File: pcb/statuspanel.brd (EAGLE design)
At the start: 57.1 x 66 mm, 8 parts

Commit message: Bump the version number.
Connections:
- net GND: now also DISPLAY.39
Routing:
- net GND: track 81.1 -> 89.8 mm
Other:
- board text added: "StatusPanel v0.3"
- board text removed: "StatusPanel v0.2"
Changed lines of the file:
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@@
 <hole x="21.59" y="4.445" drill="2.54"/>
 <hole x="3.81" y="4.445" drill="2.54"/>
-<text x="55.88" y="40.64" size="1.778" layer="25" rot="R90">StatusPanel v0.2</text>
+<text x="55.88" y="40.64" size="1.778" layer="25" rot="R90">StatusPanel v0.3</text>
 <hole x="53.34" y="62.23" drill="2.54"/>
 <hole x="53.34" y="3.81" drill="2.54"/>
@@
 <wire x1="29.2608" y1="44.3484" x2="29.21" y2="44.45" width="0.1524" layer="1"/>
 <wire x1="31.6992" y1="39.4716" x2="31.75" y2="39.37" width="0.1524" layer="1"/>
+<contactref element="DISPLAY" pad="39"/>
+<wire x1="31.6992" y1="56.0832" x2="31.6992" y2="57.15" width="0.1524" layer="1"/>
+<wire x1="30.3276" y1="54.7116" x2="31.6992" y2="56.0832" width="0.1524" layer="1"/>
+<wire x1="30.3276" y1="50.5968" x2="30.3276" y2="54.7116" width="0.1524" layer="1"/>
+<wire x1="29.2608" y1="49.53" x2="30.3276" y2="50.5968" width="0.1524" layer="1"/>
+<wire x1="31.6992" y1="57.15" x2="31.75" y2="57.15" width="0.1524" layer="1"/>
+<wire x1="29.2608" y1="49.53" x2="29.21" y2="49.53" width="0.1524" layer="1"/>
 </signal>
 <signal name="AUTO">

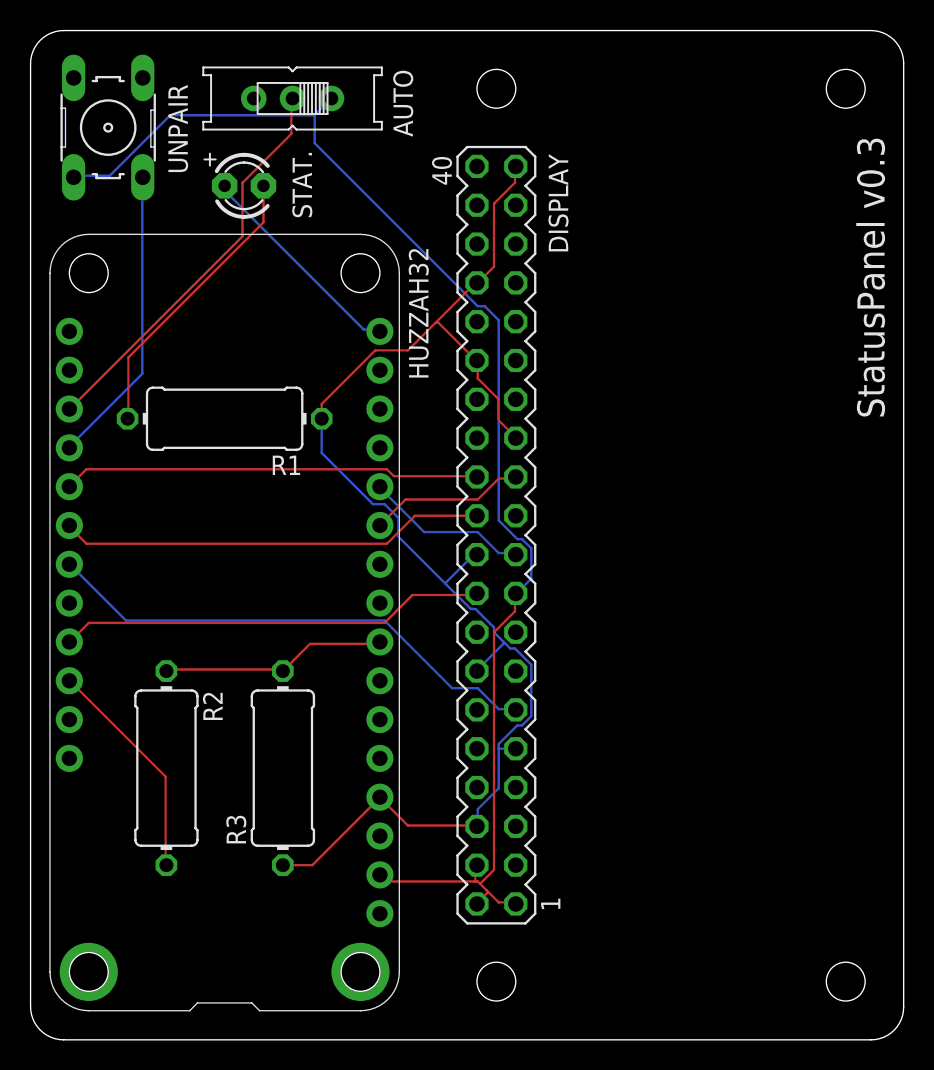
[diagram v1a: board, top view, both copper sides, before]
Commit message: Change the busy pin.
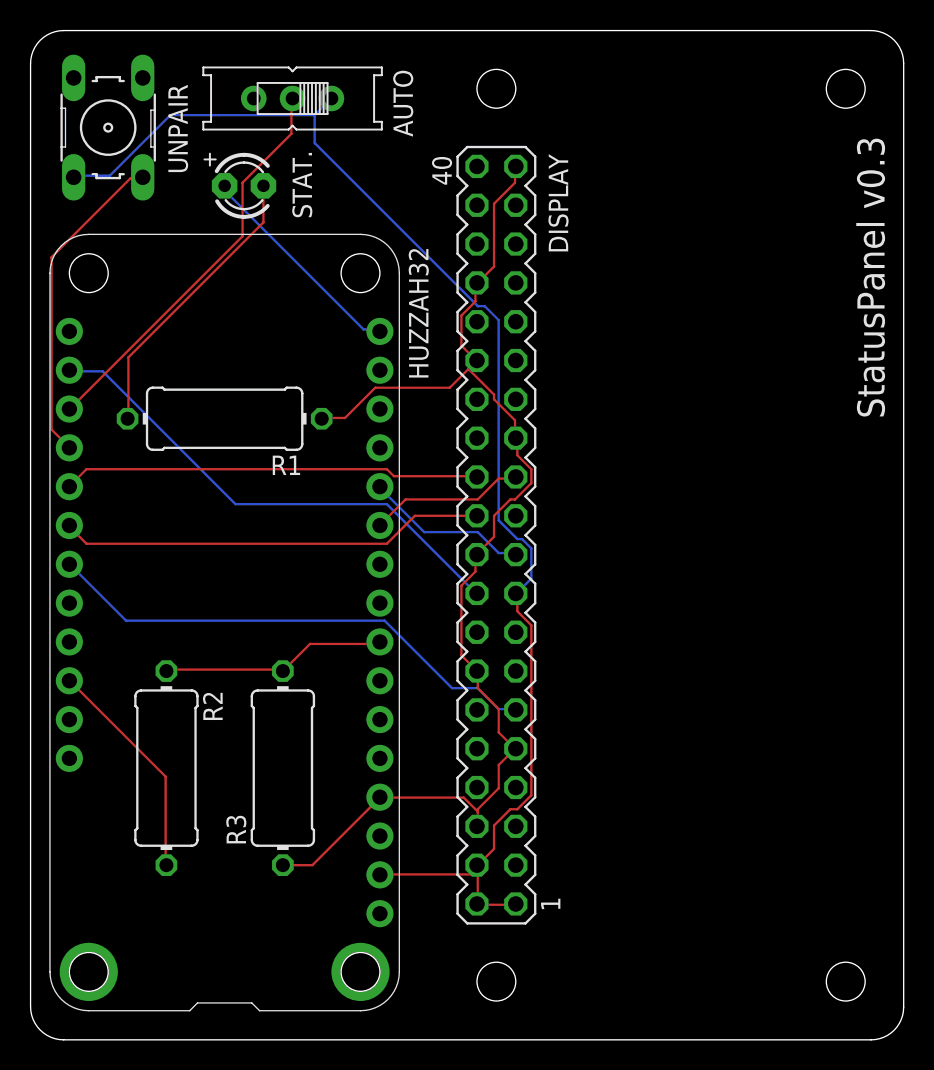
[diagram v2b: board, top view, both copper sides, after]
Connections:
- net BUSY: now also HUZZAH32.18; no longer HUZZAH32.25
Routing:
- net GND: track 89.8 -> 77.7 mm
- net BUSY: track 28.0 -> 32.7 mm
- net UNPAIR: track 19.7 -> 21.1 mm

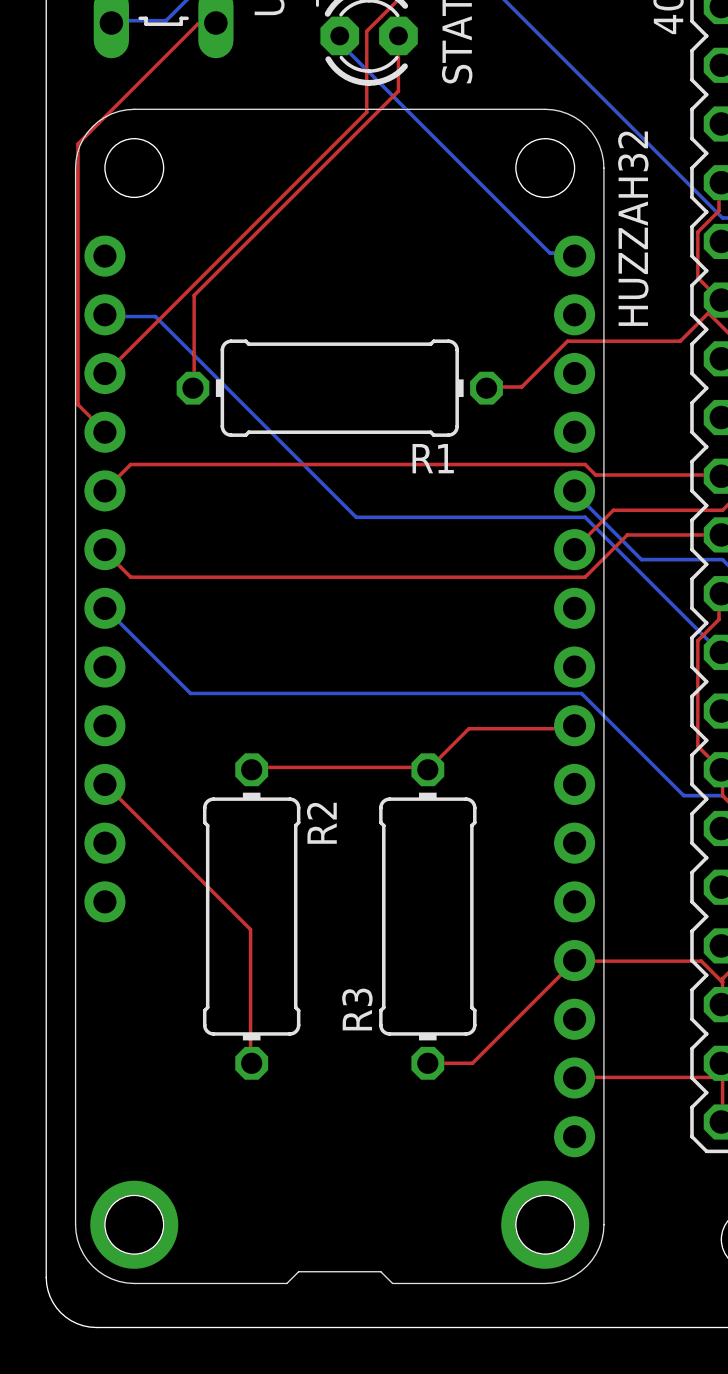
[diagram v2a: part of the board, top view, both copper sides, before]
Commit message: This corrects the pin names on the huzzah32 but makes no other changes.
Adds a new eagle library tomscis_huzzah32.lbr with the updated
component in. Note even though I removed the through holes from the
FEATHERWING_NODIM footprint, they still appear on the statuspanel
board layout. I can remove them there too if desired?
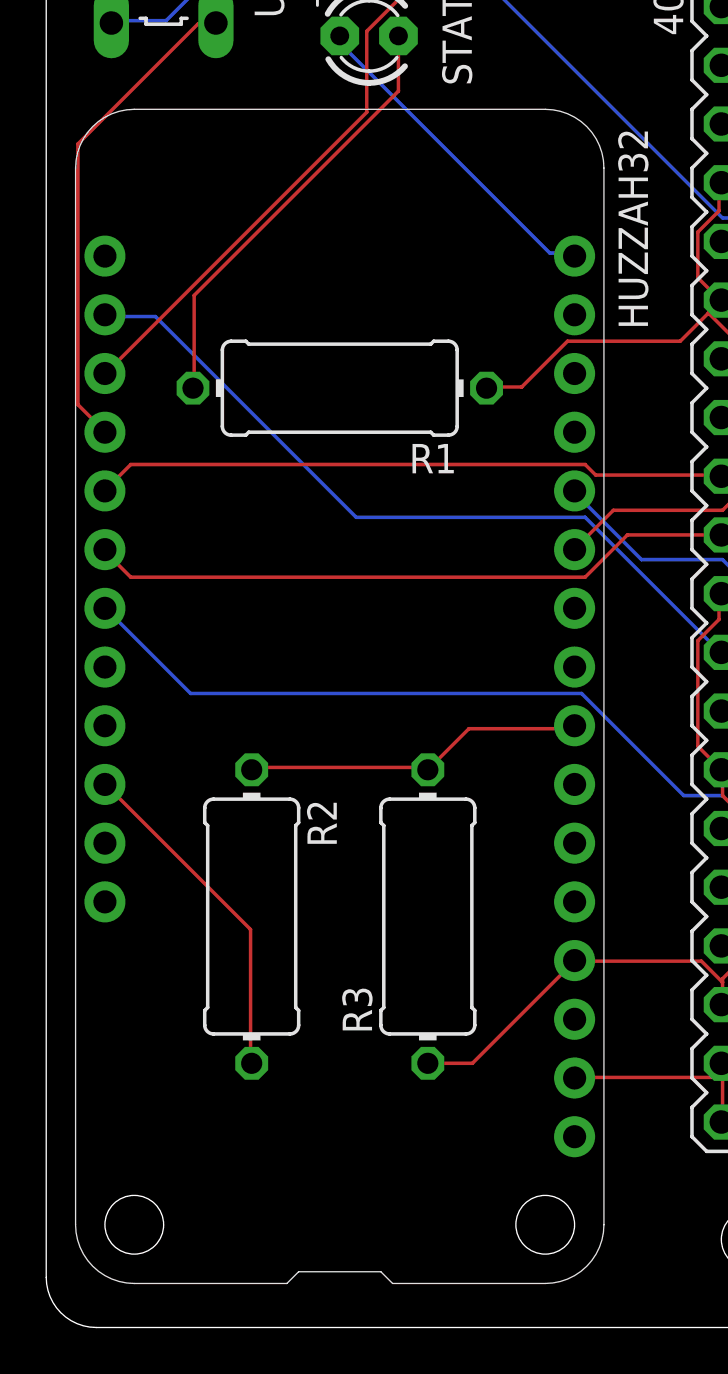
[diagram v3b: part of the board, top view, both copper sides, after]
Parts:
- HUZZAH32: value FEATHERWING_NODIM -> HUZZAH32_NODIM; device adafruit:FEATHERWING_DIM -> tomscis_huzzah32:FEATHERWING_DIM
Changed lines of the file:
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@@
 <layer number="1" name="Top" color="4" fill="1" visible="yes" active="yes"/>
 <layer number="2" name="Route2" color="16" fill="1" visible="no" active="no"/>
+<layer number="3" name="Route3" color="4" fill="3" visible="no" active="yes"/>
+<layer number="4" name="Route4" color="1" fill="4" visible="no" active="yes"/>
+<layer number="5" name="Route5" color="4" fill="4" visible="no" active="yes"/>
+<layer number="6" name="Route6" color="1" fill="8" visible="no" active="yes"/>
+<layer number="7" name="Route7" color="4" fill="8" visible="no" active="yes"/>
+<layer number="8" name="Route8" color="1" fill="2" visible="no" active="yes"/>
+<layer number="9" name="Route9" color="4" fill="2" visible="no" active="yes"/>
+<layer number="10" name="Route10" color="1" fill="7" visible="no" active="yes"/>
+<layer number="11" name="Route11" color="4" fill="7" visible="no" active="yes"/>
+<layer number="12" name="Route12" color="1" fill="5" visible="no" active="yes"/>
+<layer number="13" name="Route13" color="4" fill="5" visible="no" active="yes"/>
+<layer number="14" name="Route14" color="1" fill="6" visible="no" active="yes"/>
 <layer number="15" name="Route15" color="23" fill="1" visible="no" active="no"/>
 <layer number="16" name="Bottom" color="1" fill="1" visible="yes" active="yes"/>
@@
 <attribute name="VALUE" x="34.671" y="45.72" size="1.27" layer="27" ratio="10" rot="R90"/>
 </element>
-<element name="HUZZAH32" library="adafruit" library_urn="urn:adsk.eagle:library:420" package="FEATHERWING_DIM" value="FEATHERWING_NODIM" x="24.13" y="1.905" smashed="yes" rot="R90"/>
+<element name="HUZZAH32" library="tomscis_huzzah32" package="FEATHERWING_DIM" value="HUZZAH32_NODIM" x="24.13" y="1.905" smashed="yes" rot="R90"/>
 <element name="AUTO" library="adafruit" library_urn="urn:adsk.eagle:library:420" package="EG1218" package3d_urn="urn:adsk.eagle:package:6240649/1" value="" x="17.145" y="61.595" smashed="yes" rot="R180">
 <attribute name="NAME" x="23.749" y="63.5" size="1.27" layer="25" font="vector" rot="R270"/>
